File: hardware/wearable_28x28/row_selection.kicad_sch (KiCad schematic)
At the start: 101 parts, among them Q201 AO3403, Q202 AO3403, Q203 AO3403, Q204 AO3403, Q205 AO3403, Q206 AO3403, Q207 AO3403, Q208 AO3403, Q209 AO3403, Q210 AO3403, Q211 AO3403, Q212 AO3403, Q213 AO3403, Q214 AO3403, Q215 AO3403, Q216 AO3403, Q217 AO3403, Q218 AO3403, Q219 AO3403, Q220 AO3403, Q221 AO3403, Q222 AO3403, Q223 AO3403, Q224 AO3403, Q225 AO3403, Q226 AO3403, Q227 AO3403, Q228 AO3403, U201 SN74LVC8T245RHLR, U202 74HC154PW,118, U203 74HC154PW,118

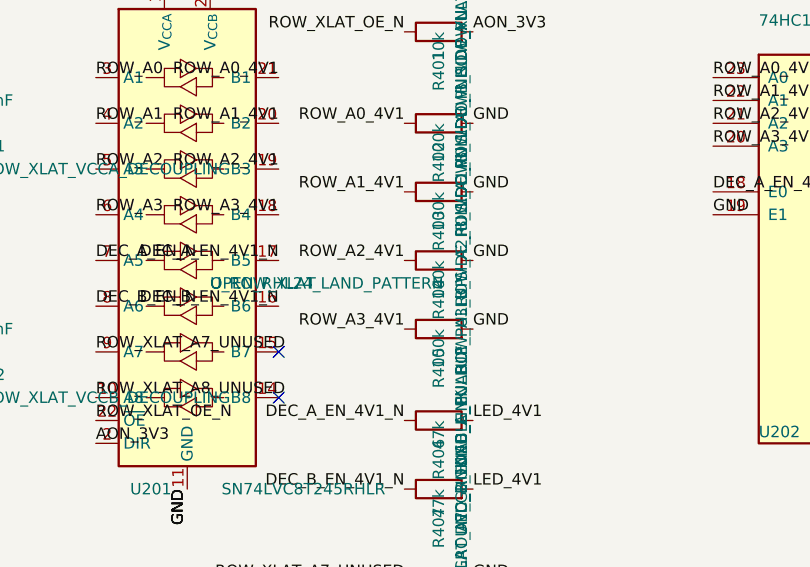
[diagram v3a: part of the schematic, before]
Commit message: Freeze mechanical inputs and RHL footprint
Co-authored-by: illiapliukhin <illiapliukhin@users.noreply.github.com>
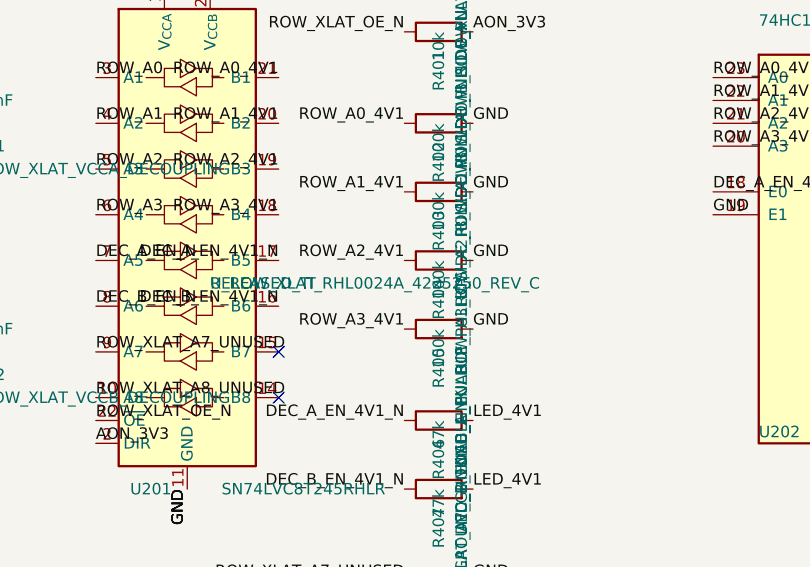
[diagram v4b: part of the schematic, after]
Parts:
- U201: footprint (none) -> PartSignal_Packages:TI_RHL0024A_VQFN-24-1EP_3.5x5.5mm_P0.5mm_EP2.05x4.05mm; FootprintStatus OPEN_RHL24_LAND_PATTERN -> RELEASED_TI_RHL0024A_4225250_REV_C
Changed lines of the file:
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@@
 			)
 		)
-		(property "Footprint" ""
+		(property "Footprint" "PartSignal_Packages:TI_RHL0024A_VQFN-24-1EP_3.5x5.5mm_P0.5mm_EP2.05x4.05mm"
 			(at 76.2 31.75 0)
 			(hide yes)
@@
 			)
 		)
-		(property "FootprintStatus" "OPEN_RHL24_LAND_PATTERN"
+		(property "FootprintStatus" "RELEASED_TI_RHL0024A_4225250_REV_C"
 			(at 58.42 60.9599 0)
 			(show_name no)

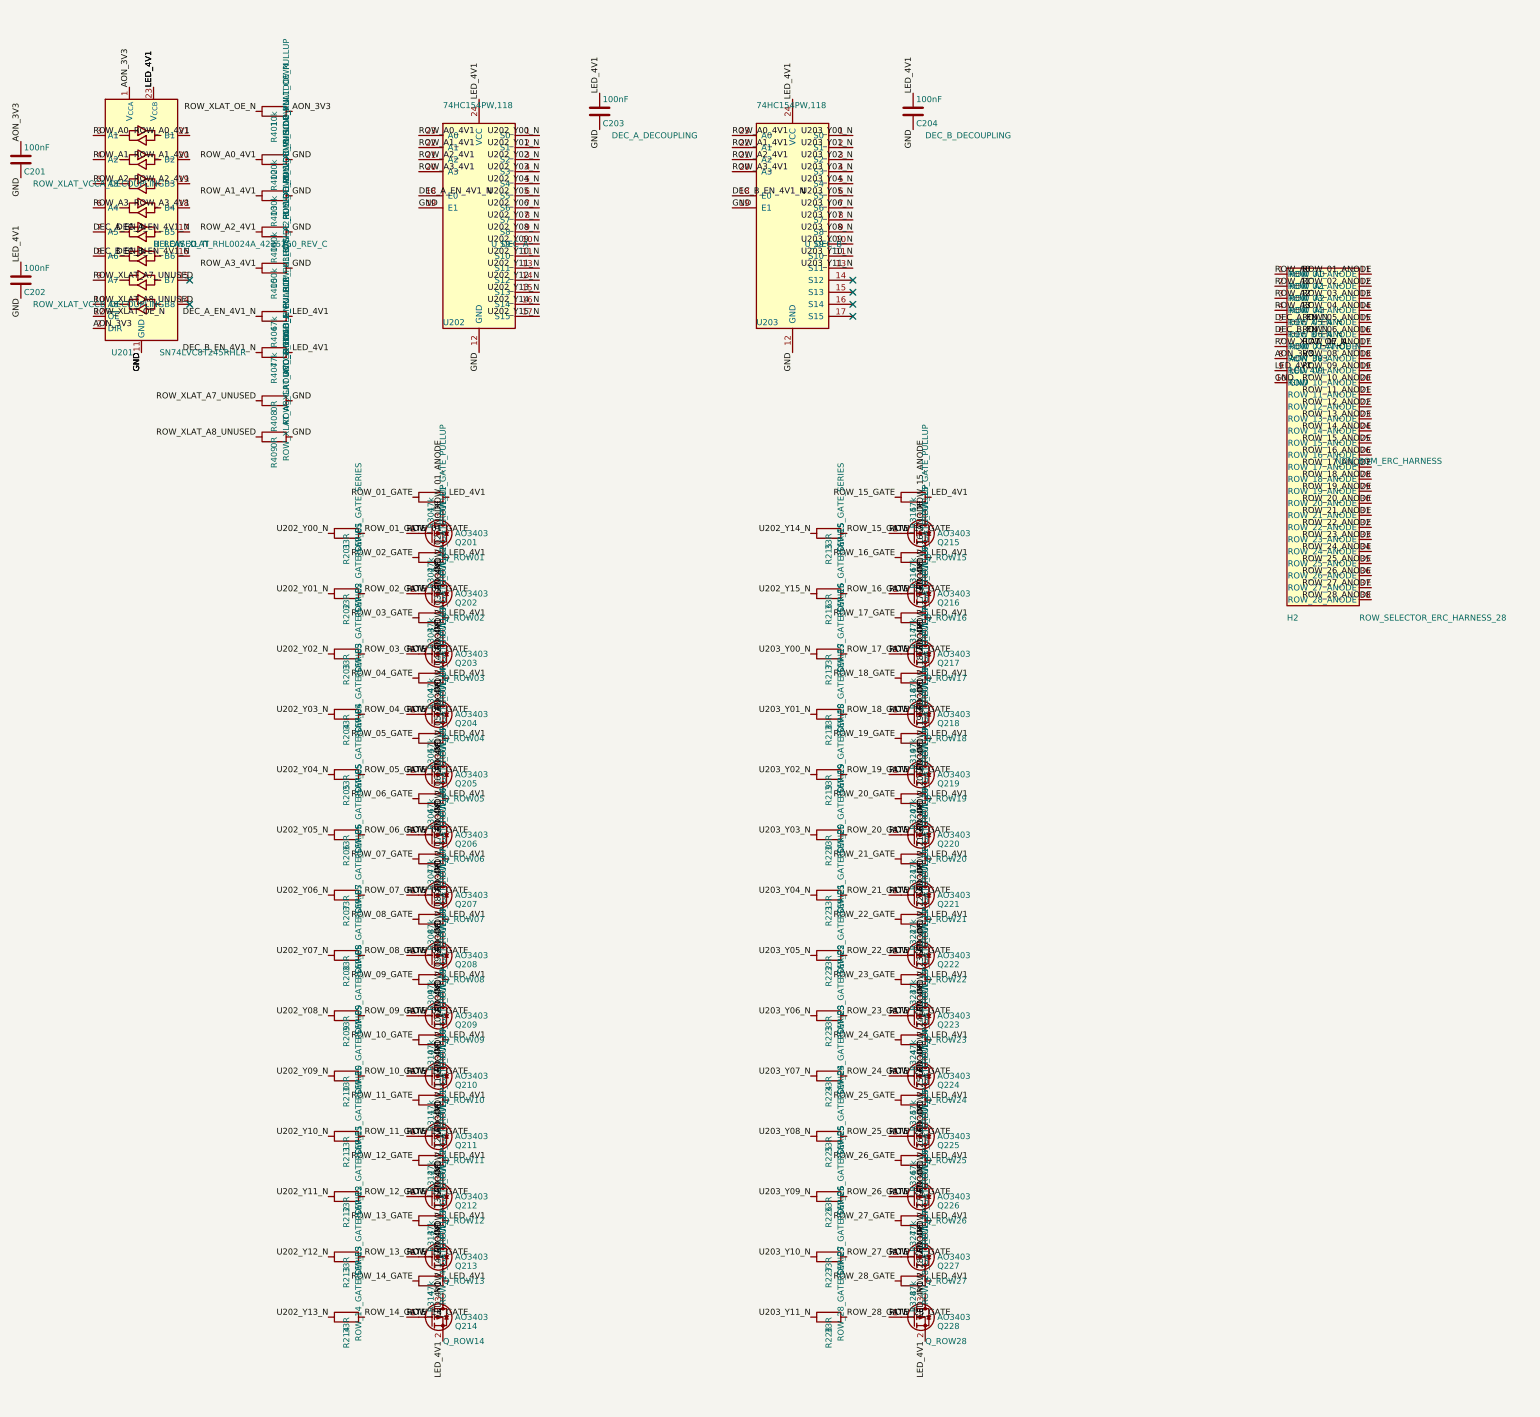
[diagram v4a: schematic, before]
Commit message: Generate complete conditional schematic hierarchy
Co-authored-by: illiapliukhin <illiapliukhin@users.noreply.github.com>
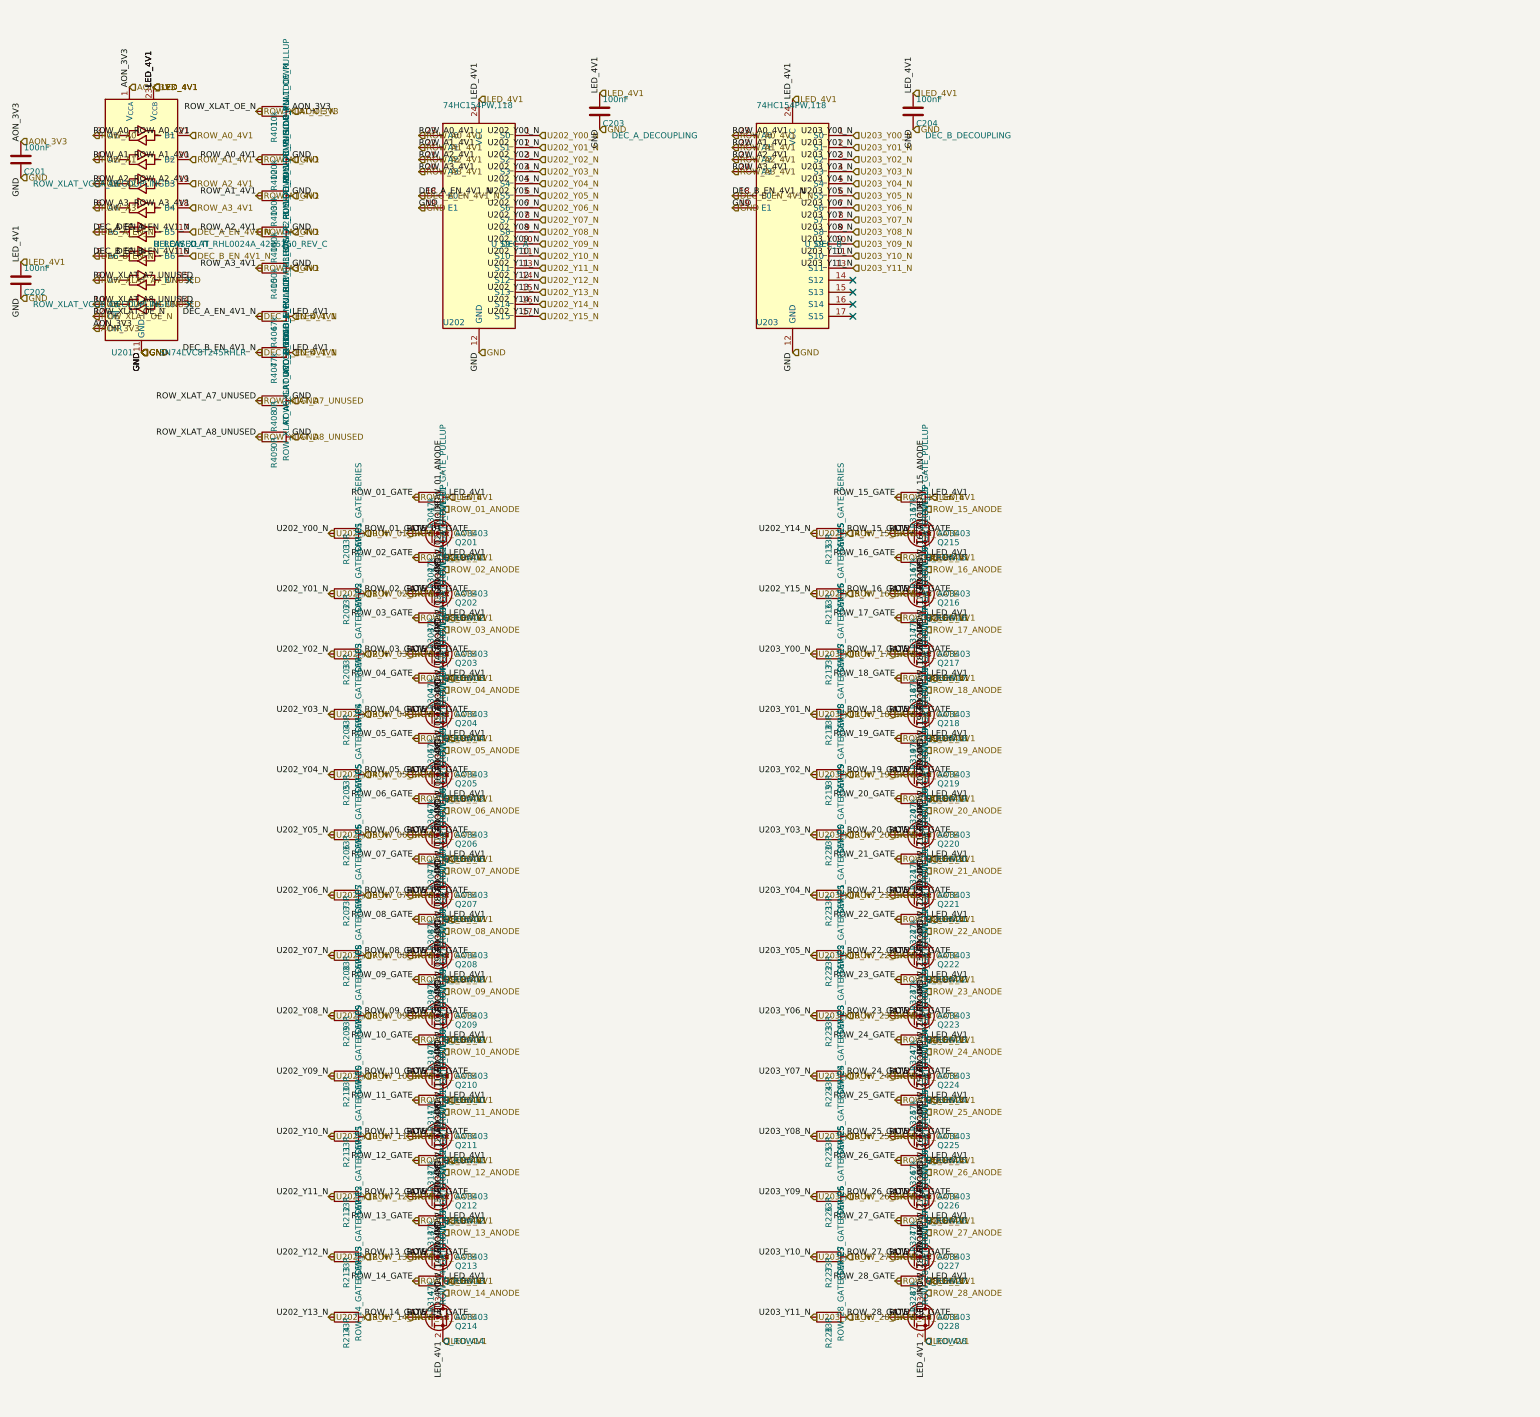
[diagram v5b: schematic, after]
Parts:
- removed H2: ROW_SELECTOR_ERC_HARNESS_28, symbol PartSignal_Wearable:ROW_SELECTOR_ERC_HARNESS_28
